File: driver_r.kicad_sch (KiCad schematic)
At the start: 35 parts, among them Q2 PNP, Q5 IRFZ48N, Q6 IRFZ48N, Q7 IRFZ48N, Q8 IRFZ48N, U5 TD340I, U6 TS922I

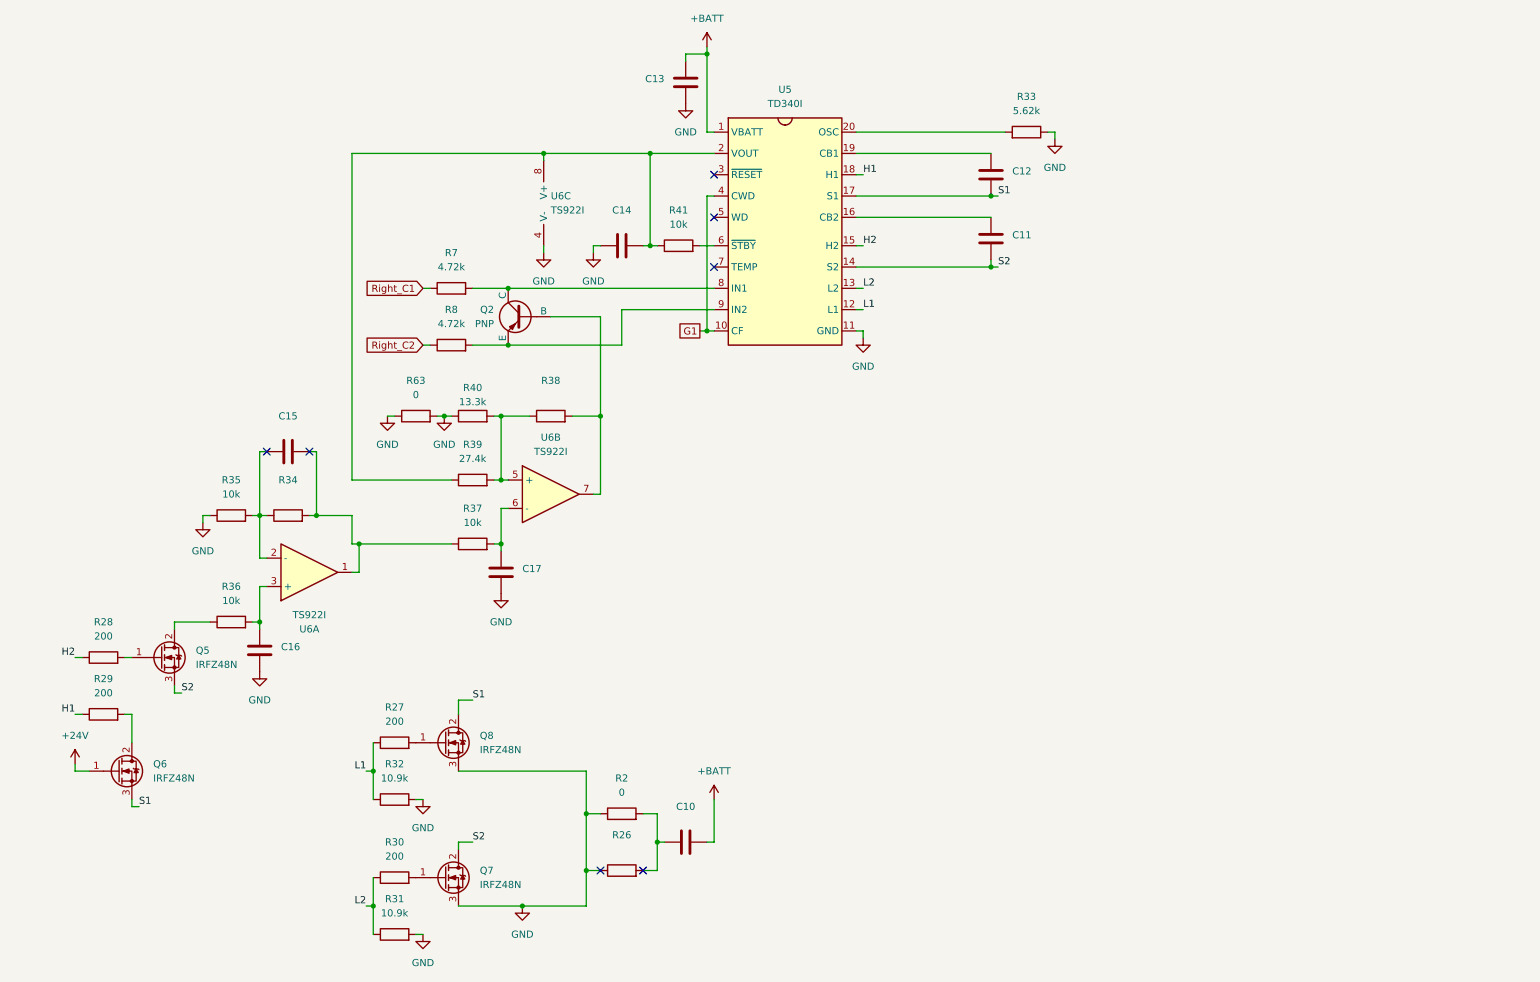
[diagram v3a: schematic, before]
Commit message: Update driver motor scheme
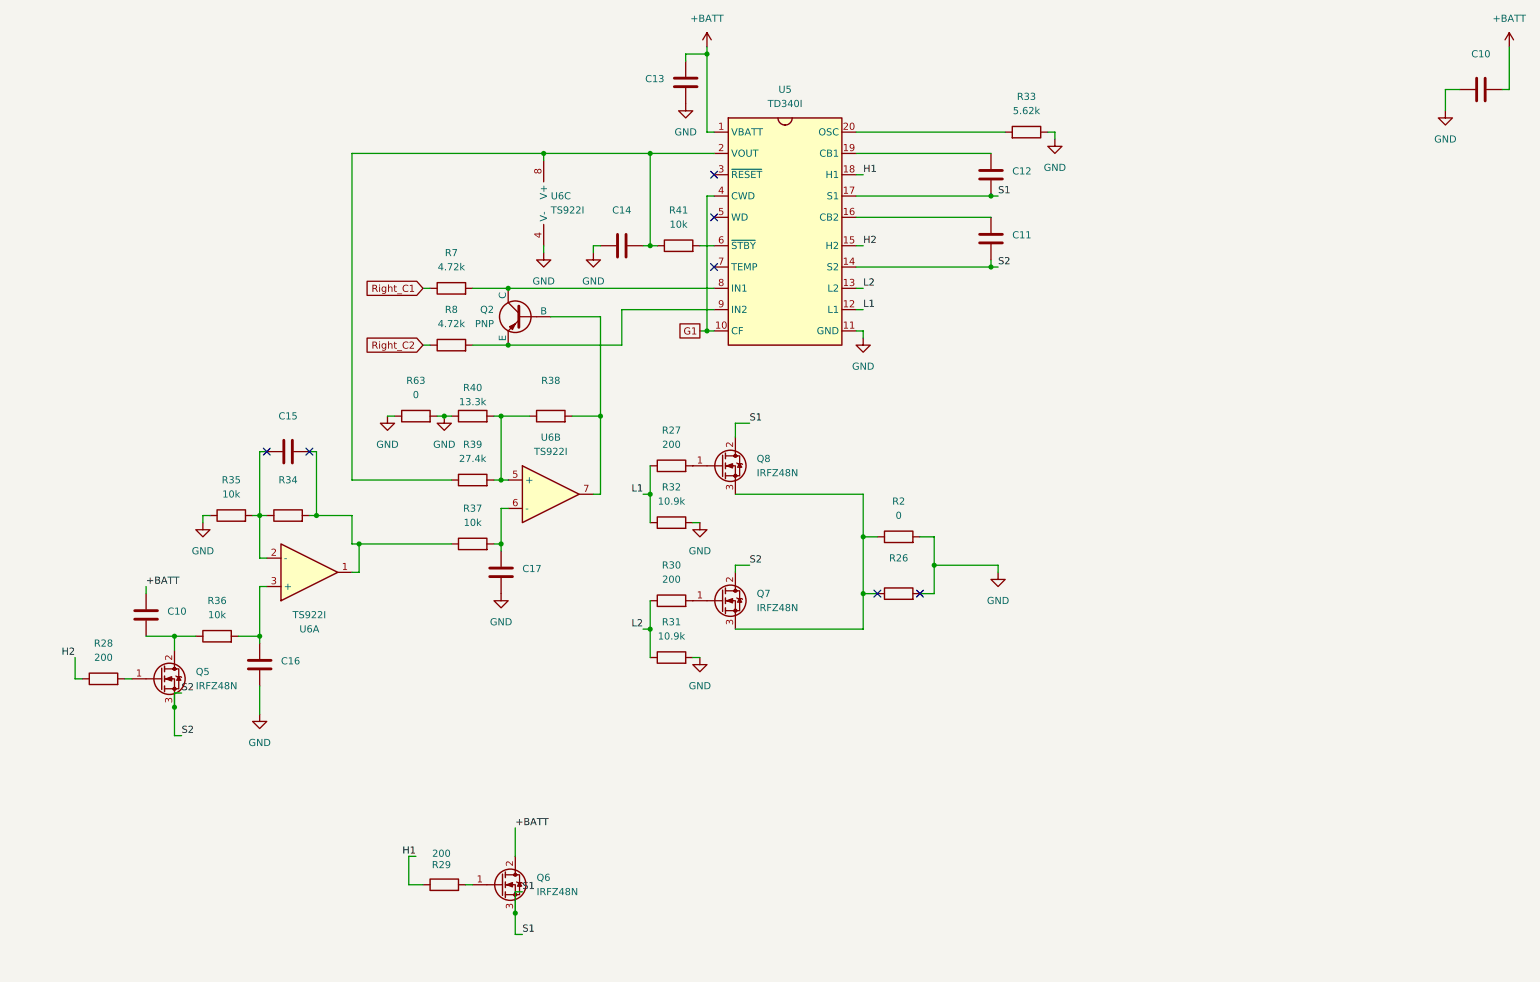
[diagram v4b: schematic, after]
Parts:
- added C10: ~, symbol Device:C
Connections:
- net +24V is gone; now on an unnamed net: Q6.1 (G)
- net +BATT: now also Q6.2 (D), C10.1
- net GND: now also C10.1, R2.2, R26.2; no longer Q7.3 (S), Q8.3 (S), R2.1, R26.1
- net at R29.2: no longer Q6.2 (D)
- net at Q5.2 (D), R36.1: now also C10.2
- new net: Q7.3 (S), Q8.3 (S), R2.1, R26.1
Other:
- moved on the sheet: C10, C16, Q5, Q6, Q7, Q8, R2, R26, R27, R28, R29, R30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

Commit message: Upgrad left driver scheme
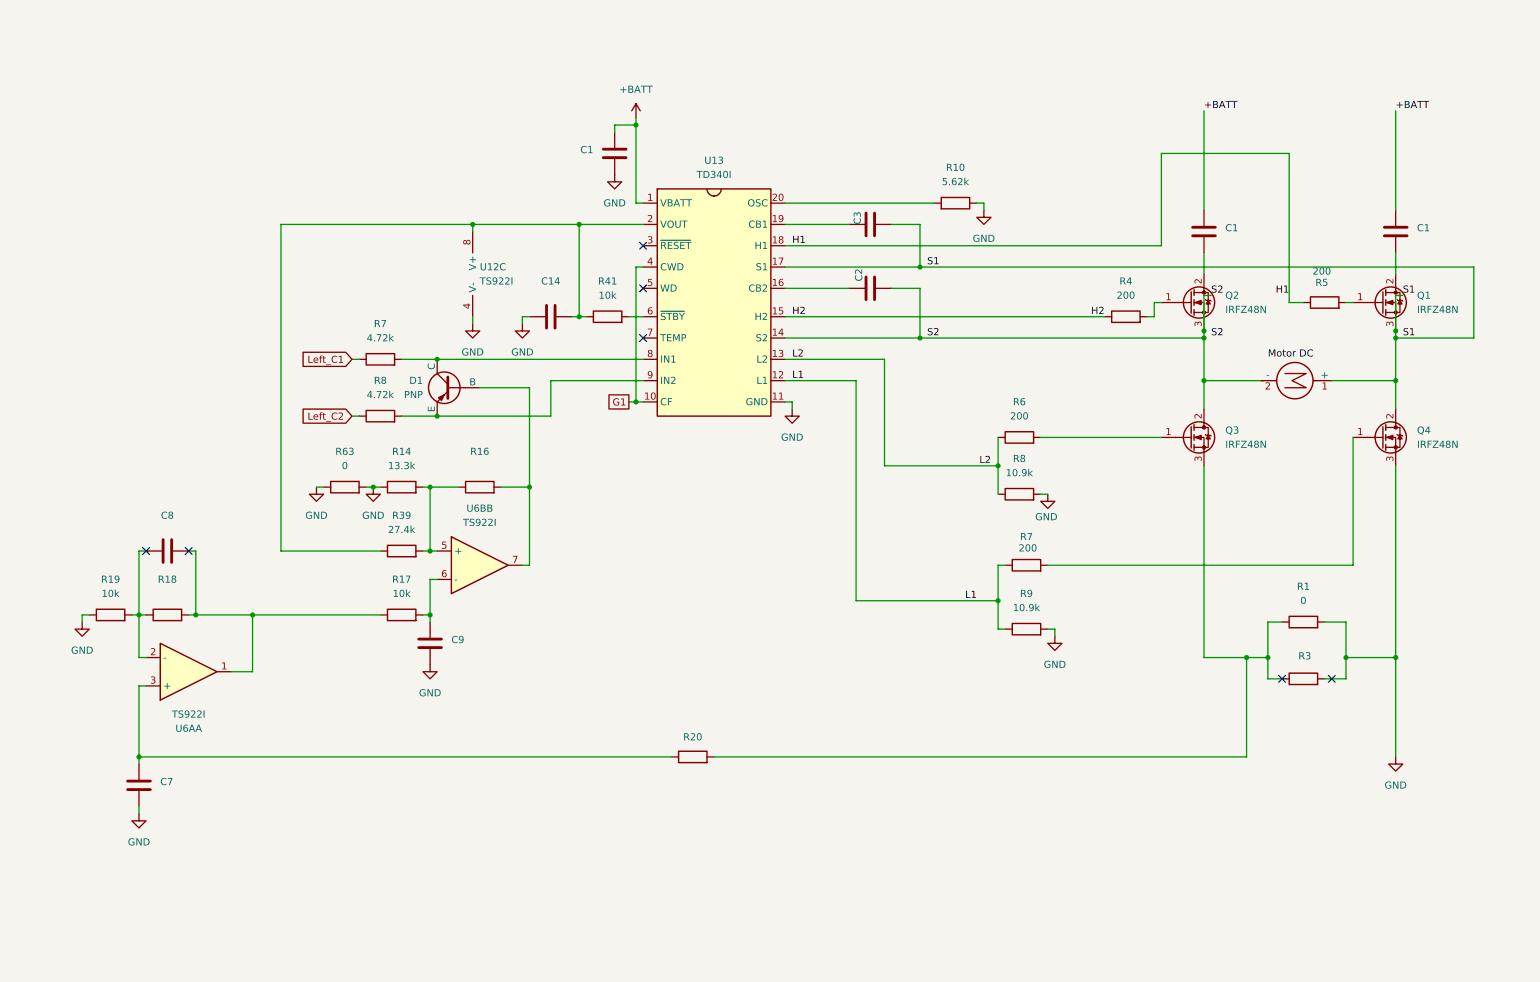
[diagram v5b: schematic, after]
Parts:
- removed C10 (x2), C11, C12, C13, C15, C16, C17: ~, symbol Device:C
- removed Q2: PNP, symbol Simulation_SPICE:PNP
- removed Q5, Q6, Q7, Q8: IRFZ48N, symbol Pioneer:IRFZ48N
- removed R2: 0, symbol Device:R
- removed R26, R34, R38: ~, symbol Device:R
- removed R27, R28, R29, R30: 200, symbol Device:R
- removed R31, R32: 10.9k, symbol Device:R
- removed R33: 5.62k, symbol Device:R
- removed R35, R36, R37: 10k, symbol Device:R
- removed R40: 13.3k, symbol Device:R
- removed R7, R8: 4.72k, symbol Device:R
- removed U5: TD340I, symbol Pioneer:TD340I
- removed U6: TS922I, symbol Device:Opamp_Dual
- added C1 (x3), C2, C3, C7, C8, C9: ~, symbol Device:C
- added D1: PNP, symbol Simulation_SPICE:PNP
- added M1: Motor_DC, symbol Motor:Motor_DC
- added Q1, Q2, Q3, Q4: IRFZ48N, symbol Pioneer:IRFZ48N
- added R1, R20: 0, symbol Device:R
- added R10: 5.62k, symbol Device:R
- added R14: 13.3k, symbol Device:R
- added R16, R18, R3: ~, symbol Device:R
- added R17, R19: 10k, symbol Device:R
- added R4, R5, R6, R7: 200, symbol Device:R
- added R7, R8: 4.72k, symbol Device:R
- added R8, R9: 10.9k, symbol Device:R
- added U12, U6A, U6B: TS922I, symbol Device:Opamp_Dual
- added U13: TD340I, symbol Pioneer:TD340I
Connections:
- net +BATT: now also C1.1, C1.1, C1.1, U13.1 (VBATT)
- net G1: now also U13.10 (CF), U13.4 (CWD)
- net GND: now also C1.2, C7.2, C9.2, Q4.3 (S), R1.2, R10.1, R14.1, R19.1, R3.2, R8.2, R9.2, U12.4 (V-), U13.11 (GND)
- net H1: now also R5.1, U13.18 (H1)
- net H2: now also R4.1, U13.15 (H2)
- net L1: now also R7.1, R9.1, U13.12 (L1)
- net L2: now also R6.1, R8.1, U13.13 (L2)
- net S1: now also C3.2, M1.1 (+), Q1.3 (S), Q4.2 (D), U13.17 (S1)
- net S2: now also C2.2, M1.2 (-), Q2.3 (S), Q3.2 (D), U13.14 (S2)
- net at C14.1, R39.1, R41.1: now also U12.8 (V+), U13.2 (VOUT)
- net at R39.2: now also R14.2, R16.1, U6B.5 (+)
- net at R41.2: now also U13.6 (~{STBY})
- new net: C8.1, R18.1, R19.2, U6A.2 (-)
- new net: C1.2, Q1.2 (D)
- new net: C9.1, R17.2, U6B.6 (-)
- new net: Q3.1 (G), R6.2
- new net: Q1.1 (G), R5.2
- new net: C2.1, U13.16 (CB2)
- new net: D1.3 (E), R8.2, U13.9 (IN2)
- new net: C7.1, R20.1, U6A.3 (+)
- new net: R10.2, U13.20 (OSC)
- new net: C8.2, R17.1, R18.2, U6A.1
- new net: D1.2 (B), R16.2, U6B.7
- new net: C3.1, U13.19 (CB1)
- new net: D1.1 (C), R7.2, U13.8 (IN1)
- new net: Q3.3 (S), R1.1, R20.2, R3.1
- new net: C1.2, Q2.2 (D)
- new net: Q2.1 (G), R4.2
- new net: Q4.1 (G), R7.2
- new net Left_C1: R7.1
- new net Left_C2: R8.1
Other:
- title: Right Driver -> LeftDriver

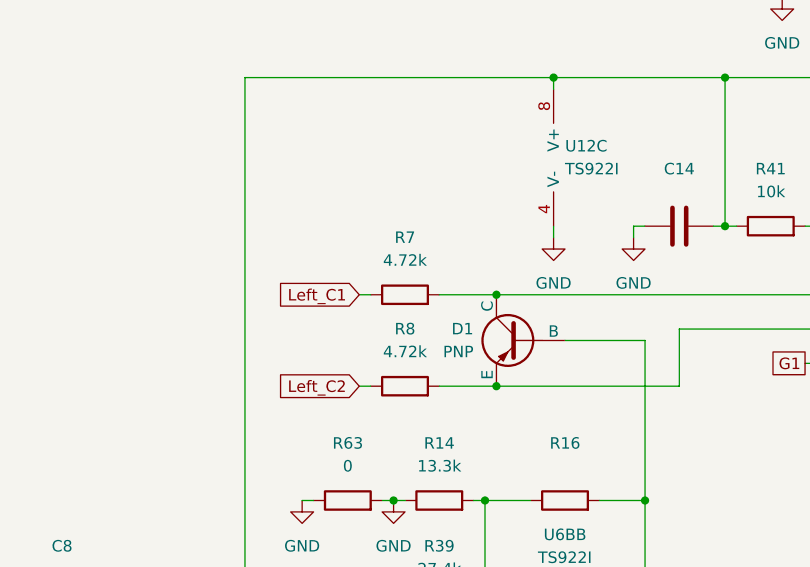
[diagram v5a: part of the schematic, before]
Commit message: Update J28 pin name
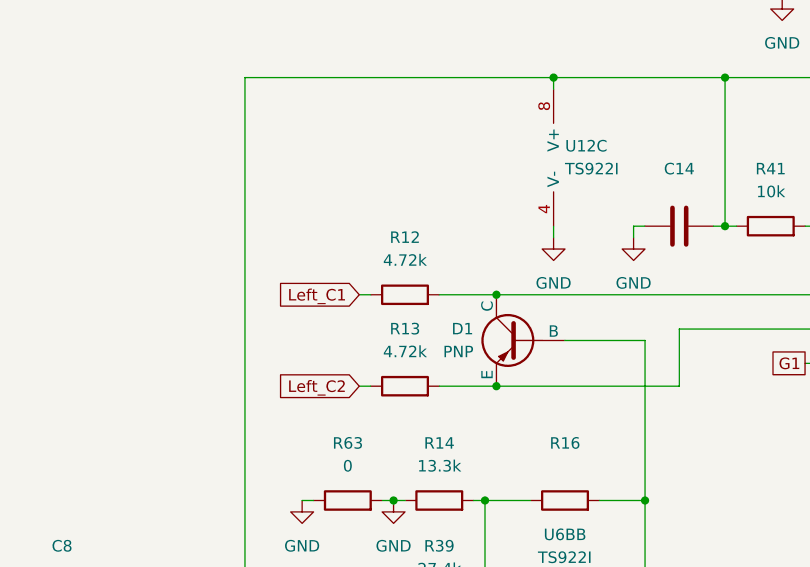
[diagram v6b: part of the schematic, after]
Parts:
- renumbered R7 to R12, R8 to R13
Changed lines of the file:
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@@
 		(dnp no)
 		(fields_autoplaced yes)
-		(property "Reference" "R8"
+		(property "Reference" "R13"
 			(at 77.47 80.01 90)
 			(effects
@@
 			(project "p3dx"
 				(path "/d0830b7c-35c9-4293-a1d2-d544311c2c60/214798ba-40d8-4782-9dce-608d1e8a9650"
-					(reference "R8")
+					(reference "R13")
 					(unit 1)
 				)
@@
 		(dnp no)
 		(fields_autoplaced yes)
-		(property "Reference" "R7"
+		(property "Reference" "R12"
 			(at 77.47 69.85 90)
 			(effects
@@
 			(project "p3dx"
 				(path "/d0830b7c-35c9-4293-a1d2-d544311c2c60/214798ba-40d8-4782-9dce-608d1e8a9650"
-					(reference "R7")
-					(unit 1)
-				)
+					(reference "R12")
+					(unit 1)
+				)
